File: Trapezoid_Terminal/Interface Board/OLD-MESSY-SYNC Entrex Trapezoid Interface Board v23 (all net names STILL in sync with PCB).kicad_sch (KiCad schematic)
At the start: 103 parts, among them P15 Conn_02x40_Odd_Even_Shielded, SW1 SW_DIP_x08

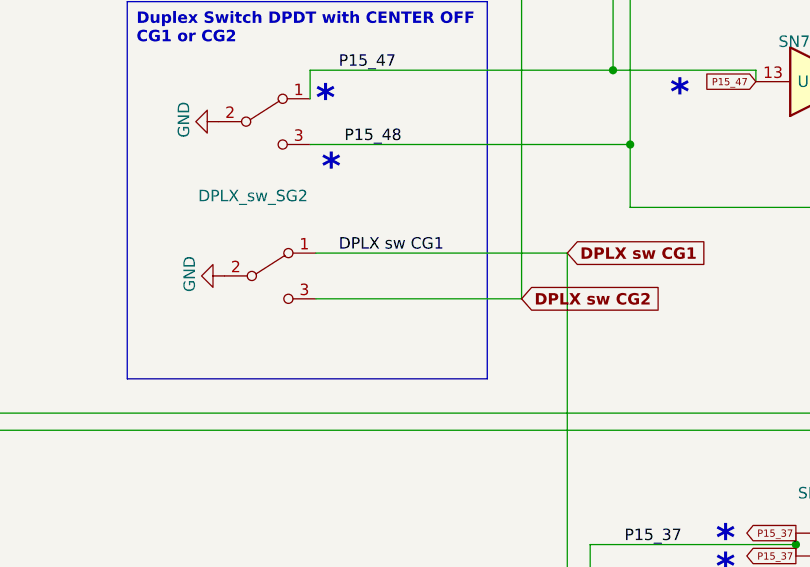
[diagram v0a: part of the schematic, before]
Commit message: Trapezoid Schematic comparisons
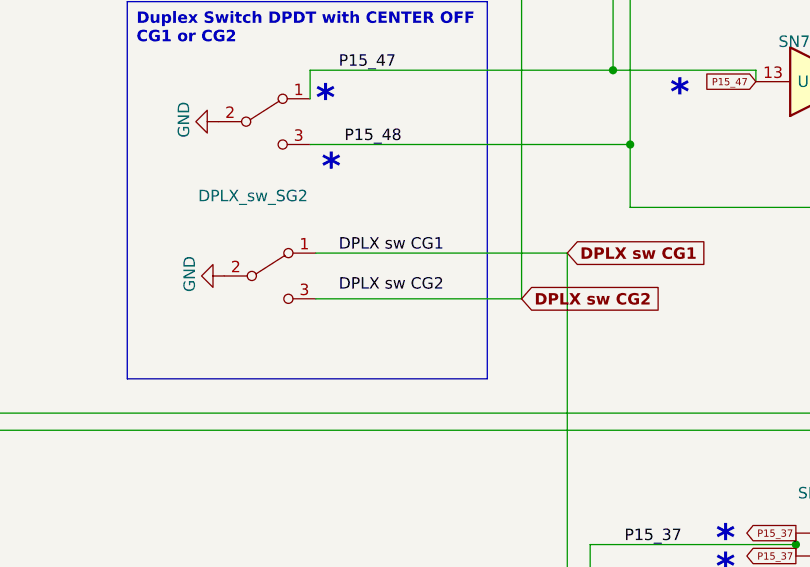
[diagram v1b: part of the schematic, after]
